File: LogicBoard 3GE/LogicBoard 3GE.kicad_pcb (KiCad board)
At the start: 4 copper layers, 103.1 x 140 mm, 159 parts, among them IC201 2363, IC202 74LS00, IC203 74LS32, IC204 2114, IC205 2114, IC206 68A09, IC207 6522, IC208 AY3-8912, IC301 MC1408, IC302 CD4052B, IC303 LF347, IC304 LF353, IC305 4066, J201 CART, J202 MD-90SM, J203 MD-90SM, J204 Power, J301 Video, J304 Conn_01x03_Pin, Q301 FMMT3905, Q302 FMMT3905, Q303 FMMT3904, SW201 Reset, Y201 6MHz

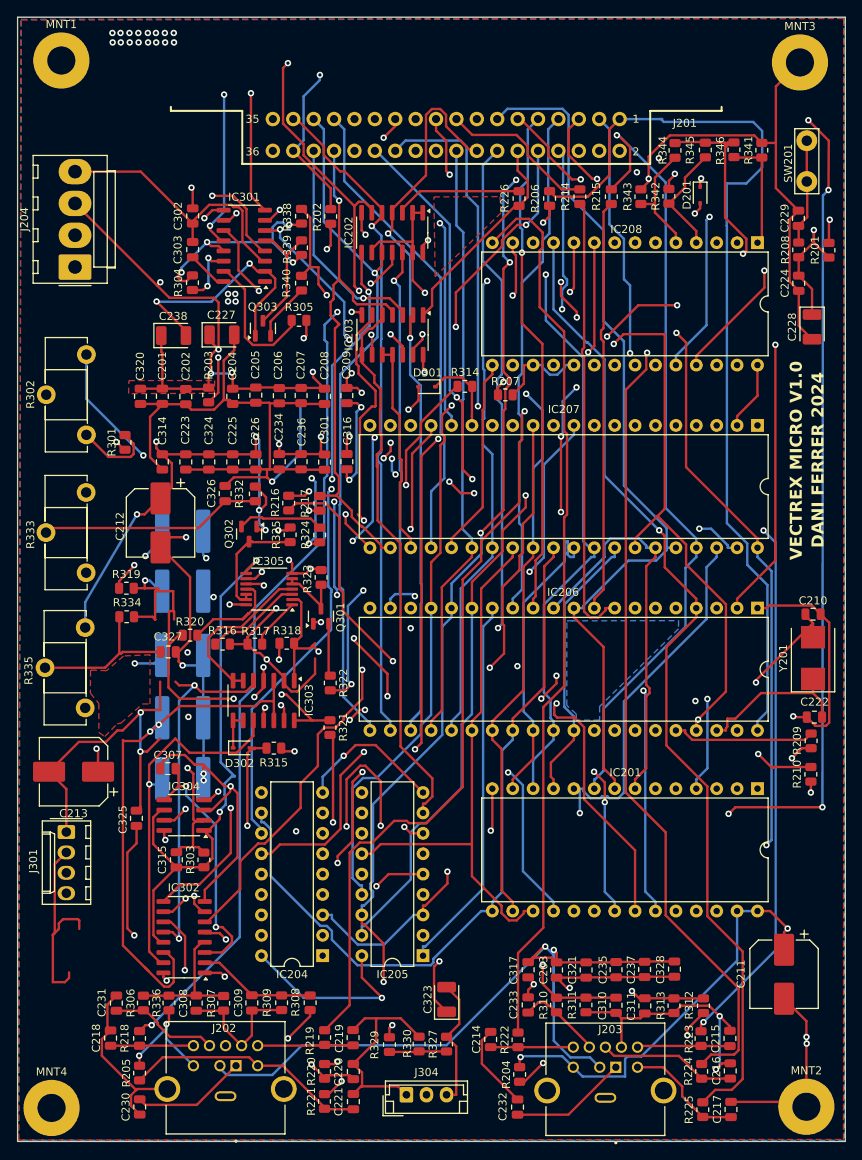
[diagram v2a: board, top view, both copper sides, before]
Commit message: added lm386 again, Added MD_90SM footprint. Solve all DRC Conflicts
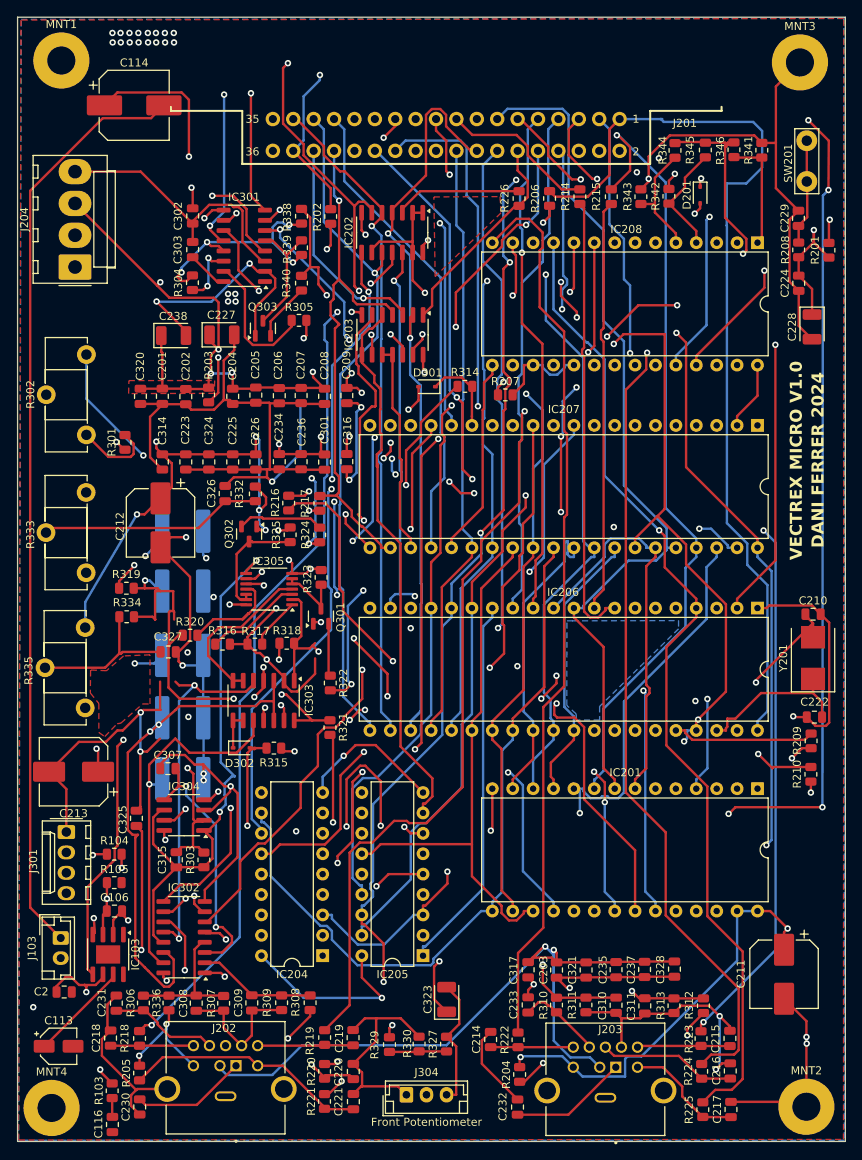
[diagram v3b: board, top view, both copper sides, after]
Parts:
- added C106: 0.22nF, Capacitor_SMD:C_0805_2012Metric, F.Cu at (60.4, 138.5)
- added C113: 10uF 16V, Capacitor_SMD:CP_Elec_4x5.3, F.Cu at (53.4, 155.3)
- added C114: 220uF 16V, Capacitor_SMD:CP_Elec_8x10.5, F.Cu at (62.8, 38.2)
- added C116: 0.1uF 50V, Capacitor_SMD:C_0805_2012Metric, F.Cu at (60.1, 165.1)
- added C2: 0.1uF 50V, Capacitor_SMD:C_0805_2012Metric, F.Cu at (54.1, 148.6)
- added IC103: LM386-3, Package_SO:SOIC-8-1EP_3.9x4.9mm_P1.27mm_EP2.29x3mm, F.Cu at (59.6, 143.9)
- added J103: Conn_01x02, Connector_JST:JST_EH_B2B-EH-A_1x02_P2.50mm_Vertical, F.Cu at (53.7, 141.9)
- added R103: 10, Resistor_SMD:R_0805_2012Metric, F.Cu at (60.1, 160.9)
- added R104: 6.8k, Resistor_SMD:R_0805_2012Metric, F.Cu at (60.3, 131.4)
- added R105: 47k, Resistor_SMD:R_0805_2012Metric, F.Cu at (60.3, 135.0)
- J304: value Conn_01x03_Pin -> Front Potentiometer
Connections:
- C201 pad 1: +5V -> /~{RESET}
- C202 pad 1: +5V -> /~{RESET}
- C204 pad 1: +5V -> /~{RESET}
- C205 pad 1: +5V -> /~{RESET}
- C206 pad 1: +5V -> /~{RESET}
- C207 pad 1: +5V -> /~{RESET}
- C208 pad 2: +5V -> /~{RESET}
- C209 pad 1: +5V -> /~{RESET}
- C211 pad 1: +5V -> /~{RESET}
- C212 pad 1: +5V -> /~{RESET}
- C223 pad 1: +5V -> /~{RESET}
- C224 pad 1: +5V -> /~{RESET}
- C225 pad 1: +5V -> /~{RESET}
- C226 pad 1: +5V -> /~{RESET}
- C227 pad 1: +5V -> /~{RESET}
- C228 pad 1: +5V -> /~{RESET}
- C234 pad 1: +5V -> /~{RESET}
- C236 pad 2: +5V -> /~{RESET}
- C238 pad 1: +5V -> /~{RESET}
- C301 pad 2: +5V -> /~{RESET}
- C312 pad 2: +5V -> /~{RESET}
- C314 pad 2: +5V -> /~{RESET}
- C316 pad 2: +5V -> /~{RESET}
- C320 pad 2: +5V -> /~{RESET}
- C324 pad 2: +5V -> /~{RESET}
- D201 pad 2: +5V -> /~{RESET}
- IC201 pad 1: +5V -> /~{RESET}
- IC201 pad 27: +5V -> /~{RESET}
- IC201 pad 28: +5V -> /~{RESET}
- IC203 pad 14: +5V -> /~{RESET}
- IC204 pad 18: +5V -> /~{RESET}
- IC205 pad 18: +5V -> /~{RESET}
- IC206 pad 37: +5V -> /~{RESET}
- IC206 pad 7: +5V -> /~{RESET}
- IC207 pad 20: +5V -> /~{RESET}
- IC207 pad 34: +5V -> /~{RESET}
- IC208 pad 16: +5V -> /~{RESET}
- IC302 pad 16: +5V -> /~{RESET}
- IC303 pad 2: +5V -> /~{RESET}
- IC303 pad 4: +5V -> /~{RESET}
- IC304 pad 8: +5V -> /~{RESET}
- IC305 pad 14: +5V -> /~{RESET}
- J202 pad 6: +5V -> /~{RESET}
- J203 pad 6: +5V -> /~{RESET}
- J204 pad 3: +5V -> /~{RESET}
- J301 pad 2: +5V -> /~{RESET}
- Q301 pad 1: +5V -> /~{RESET}
- Q302 pad 1: +5V -> /~{RESET}
- R201 pad 2: +5V -> /~{RESET}
- R203 pad 2: +5V -> /~{RESET}
- R204 pad 2: +5V -> /~{RESET}
- R205 pad 1: +5V -> /~{RESET}
- R207 pad 2: +5V -> /~{RESET}
- R208 pad 1: +5V -> /~{RESET}
- R209 pad 1: +5V -> /~{RESET}
- R210 pad 2: +5V -> /~{RESET}
- R301 pad 2: +5V -> /~{RESET}
- R316 pad 1: +5V -> /~{RESET}
- R317 pad 2: +5V -> /~{RESET}
- R318 pad 1: +5V -> /~{RESET}
- R325 pad 2: +5V -> /~{RESET}
- R332 pad 1: +5V -> /~{RESET}
- R333 pad 3: +5V -> /~{RESET}
- R335 pad 3: +5V -> /~{RESET}
- R336 pad 1: +5V -> /~{RESET}
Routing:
- net /~{RESET}: track 0.00 -> 851.6 mm, vias 0 -> 43
- net +5V: track 964.2 -> 135.5 mm, vias 74 -> 34
- net Net-(C114-Pad1): track 0.00 -> 186.7 mm, vias 0 -> 3
- net Net-(J103-Pin_1): track 0.00 -> 115.7 mm
- net GND: track 917.7 -> 942.8 mm, vias 29 -> 32
- net Net-(IC103-+): track 0.00 -> 14.7 mm, vias 0 -> 2
- net Audio: track 64.4 -> 77.2 mm, vias 1 -> 2
- net Net-(IC103-BYPASS): track 0.00 -> 12.6 mm
- net Net-(C116-Pad1): track 0.00 -> 2.35 mm
- net /X1: track 67.8 -> 66.0 mm

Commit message: updated powerlines to 5mm, solve DRC conflicts
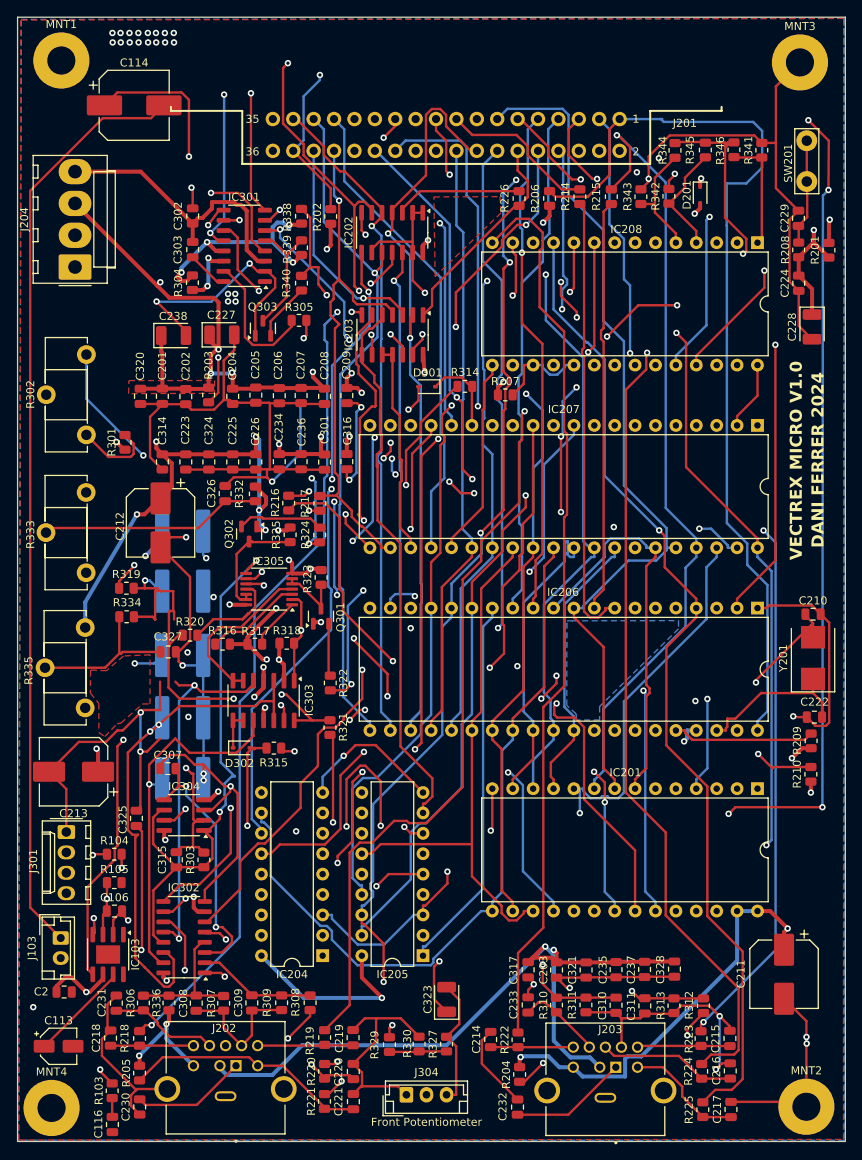
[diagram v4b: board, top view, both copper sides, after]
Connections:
- C201 pad 1: /~{RESET} -> +5V
- C202 pad 1: /~{RESET} -> +5V
- C204 pad 1: /~{RESET} -> +5V
- C205 pad 1: /~{RESET} -> +5V
- C206 pad 1: /~{RESET} -> +5V
- C207 pad 1: /~{RESET} -> +5V
- C208 pad 2: /~{RESET} -> +5V
- C209 pad 1: /~{RESET} -> +5V
- C211 pad 1: /~{RESET} -> +5V
- C212 pad 1: /~{RESET} -> +5V
- C223 pad 1: /~{RESET} -> +5V
- C224 pad 1: /~{RESET} -> +5V
- C225 pad 1: /~{RESET} -> +5V
- C226 pad 1: /~{RESET} -> +5V
- C227 pad 1: /~{RESET} -> +5V
- C228 pad 1: /~{RESET} -> +5V
- C234 pad 1: /~{RESET} -> +5V
- C236 pad 2: /~{RESET} -> +5V
- C238 pad 1: /~{RESET} -> +5V
- C301 pad 2: /~{RESET} -> +5V
- C312 pad 2: /~{RESET} -> +5V
- C314 pad 2: /~{RESET} -> +5V
- C316 pad 2: /~{RESET} -> +5V
- C320 pad 2: /~{RESET} -> +5V
- C324 pad 2: /~{RESET} -> +5V
- D201 pad 2: /~{RESET} -> +5V
- IC201 pad 1: /~{RESET} -> +5V
- IC201 pad 27: /~{RESET} -> +5V
- IC201 pad 28: /~{RESET} -> +5V
- IC203 pad 14: /~{RESET} -> +5V
- IC204 pad 18: /~{RESET} -> +5V
- IC205 pad 18: /~{RESET} -> +5V
- IC206 pad 37: /~{RESET} -> +5V
- IC206 pad 7: /~{RESET} -> +5V
- IC207 pad 20: /~{RESET} -> +5V
- IC207 pad 34: /~{RESET} -> +5V
- IC208 pad 16: /~{RESET} -> +5V
- IC302 pad 16: /~{RESET} -> +5V
- IC303 pad 2: /~{RESET} -> +5V
- IC303 pad 4: /~{RESET} -> +5V
- IC304 pad 8: /~{RESET} -> +5V
- IC305 pad 14: /~{RESET} -> +5V
- J202 pad 6: /~{RESET} -> +5V
- J203 pad 6: /~{RESET} -> +5V
- J204 pad 3: /~{RESET} -> +5V
- J301 pad 2: /~{RESET} -> +5V
- Q301 pad 1: /~{RESET} -> +5V
- Q302 pad 1: /~{RESET} -> +5V
- R201 pad 2: /~{RESET} -> +5V
- R203 pad 2: /~{RESET} -> +5V
- R204 pad 2: /~{RESET} -> +5V
- R205 pad 1: /~{RESET} -> +5V
- R207 pad 2: /~{RESET} -> +5V
- R208 pad 1: /~{RESET} -> +5V
- R209 pad 1: /~{RESET} -> +5V
- R210 pad 2: /~{RESET} -> +5V
- R301 pad 2: /~{RESET} -> +5V
- R316 pad 1: /~{RESET} -> +5V
- R317 pad 2: /~{RESET} -> +5V
- R318 pad 1: /~{RESET} -> +5V
- R325 pad 2: /~{RESET} -> +5V
- R332 pad 1: /~{RESET} -> +5V
- R333 pad 3: /~{RESET} -> +5V
- R335 pad 3: /~{RESET} -> +5V
- R336 pad 1: /~{RESET} -> +5V
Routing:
- net /~{RESET}: track 851.6 -> 0.00 mm, vias 43 -> 0
- net +5V: track 135.5 -> 865.3 mm, vias 34 -> 75
- net /IC303A_Y: track 44.3 -> 35.0 mm
- net -12VA: track 34.9 -> 36.7 mm
- net /IOUT: track 118.2 -> 119.8 mm
- net -5VA: track 164.0 -> 165.3 mm
- net GND: track 942.8 -> 941.5 mm
- net /P2: track 105.9 -> 106.9 mm
- net /P3: track 135.1 -> 135.7 mm
